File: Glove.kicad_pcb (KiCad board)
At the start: 2 copper layers, 72.8 x 52 mm, 37 parts, among them J1 USB_C_Receptacle_USB2.0, J2 Joystick, J3 Conn_01x07, J4 Conn_01x07, J5 Conn_01x06, Q1 2N7002, Q2 2N7002, U1 LM1117-3.3, U2 ESP32-WROOM-32D, U3 CP2102N-Axx-xQFN24

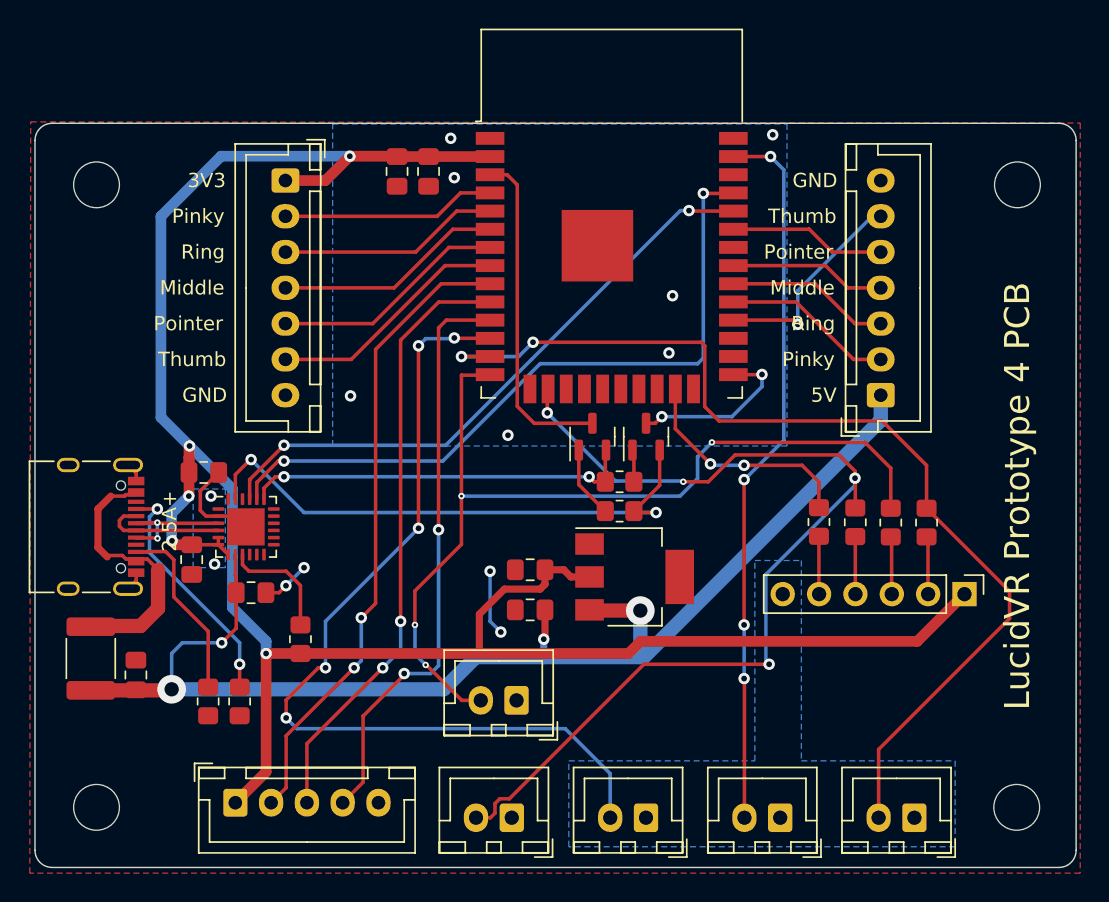
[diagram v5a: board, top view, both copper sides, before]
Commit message: Change routing of 5V and 3V3 lines
Signed-off-by: Kozova1 <mug66kk@gmail.com>
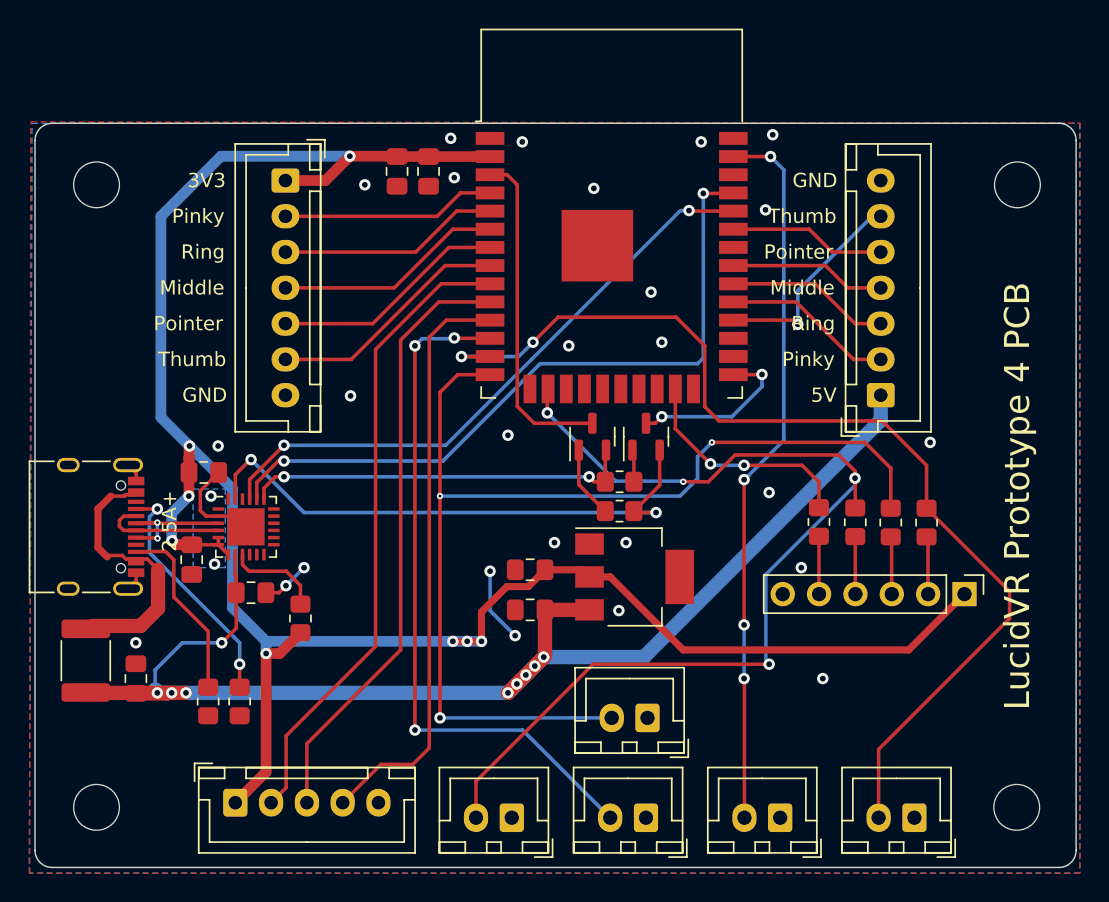
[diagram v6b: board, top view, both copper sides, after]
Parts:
- moved BTN_Trigger1 9.23 mm to (153.0, 97.8)
- moved R9 1.45 mm to (128.8, 90.8)
- moved F1 0.38 mm to (113.8, 93.8)
- moved C6 0.25 mm to (117.2, 95.0)
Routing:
- net BtnA: track 62.7 -> 48.3 mm, vias 5 -> 3
- net BtnTrigger: track 64.8 -> 76.3 mm, vias 4 -> 3
- net +5V: track 87.6 -> 93.0 mm, vias 4 -> 9
- net +3V3: track 150.9 -> 148.9 mm, vias 5 -> 8
- net Net-(R9-Pad2): track 8.11 -> 6.66 mm
- net BtnB: track 71.8 -> 73.2 mm
- net BtnGrab: track 70.0 -> 71.1 mm
- net GND: track 17.5 -> 18.2 mm, vias 13 -> 28
- net JoyClick: track 40.9 -> 41.1 mm, vias 2 -> 0
- net JoyY: vias 2 -> 0
- net JoyX: vias 2 -> 0

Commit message: Switch to QFN28 version of CP2102
Signed-off-by: Kozova1 <mug66kk@gmail.com>
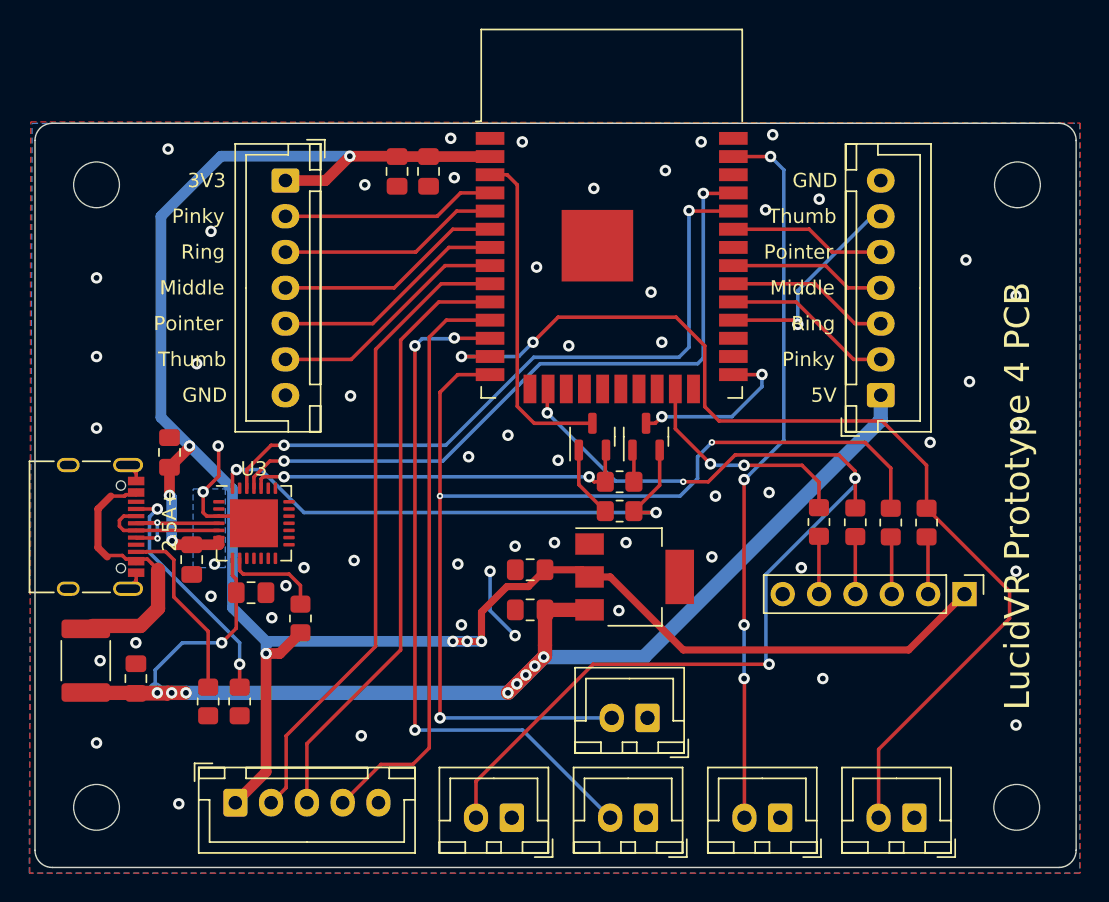
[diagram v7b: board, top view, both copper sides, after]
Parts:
- U1: value LM1117-3.3 -> LM1117S-3.3
- U3: value CP2102N-Axx-xQFN24 -> CP2102N-Axx-xQFN28; footprint Package_DFN_QFN:QFN-24-1EP_4x4mm_P0.5mm_EP2.6x2.6mm -> Package_DFN_QFN:QFN-28-1EP_5x5mm_P0.5mm_EP3.35x3.35mm
- moved C4 2.78 mm to (119.6, 79.2), turned to 90 degrees
- moved U3 0.60 mm to (125.5, 84.2)
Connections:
- U3 pad 19: Net-(Q1-Pad2) -> unconnected-(U3-Pad19)
- U3 pad 2: GND -> unconnected-(U3-Pad2)
- U3 pad 20: RXD -> unconnected-(U3-Pad20)
- U3 pad 21: TXD -> unconnected-(U3-Pad21)
- U3 pad 23: Net-(Q2-Pad2) -> unconnected-(U3-Pad23)
- U3 pad 24: unconnected-(U3-Pad24) -> Net-(Q1-Pad2)
- U3 pad 25: GND -> RXD
- U3 pad 3: /D+ -> GND
- U3 pad 4: /D- -> /D+
- U3 pad 5: +3V3 -> /D-
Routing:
- net TXD: track 43.0 -> 48.4 mm
- net +3V3: track 148.9 -> 146.8 mm
- net GND: track 18.2 -> 16.9 mm, vias 28 -> 57
- net Net-(Q2-Pad2): track 39.7 -> 38.6 mm
